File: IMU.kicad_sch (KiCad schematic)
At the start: 12 parts, among them U5 H3LIS331DLTR, U6 MMC5983MA, U7 ICM-20608-G

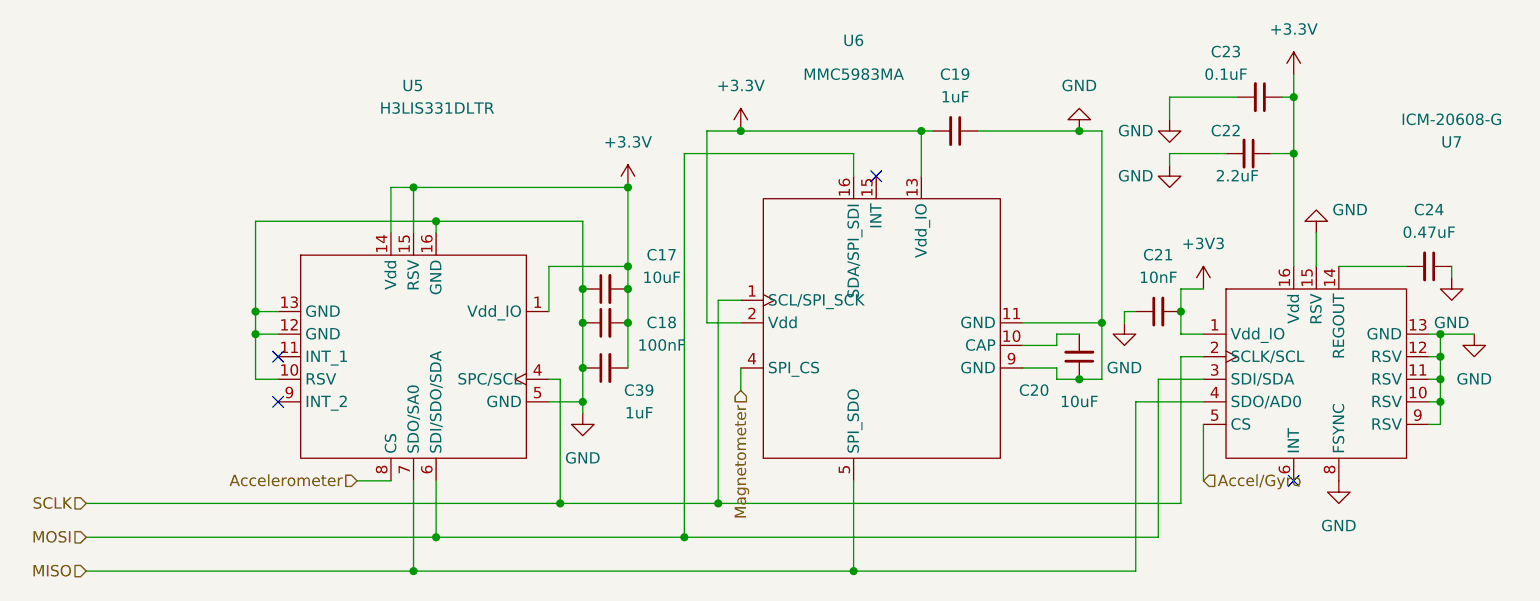
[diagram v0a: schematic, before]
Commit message: rerouted spi bus and changed NAND
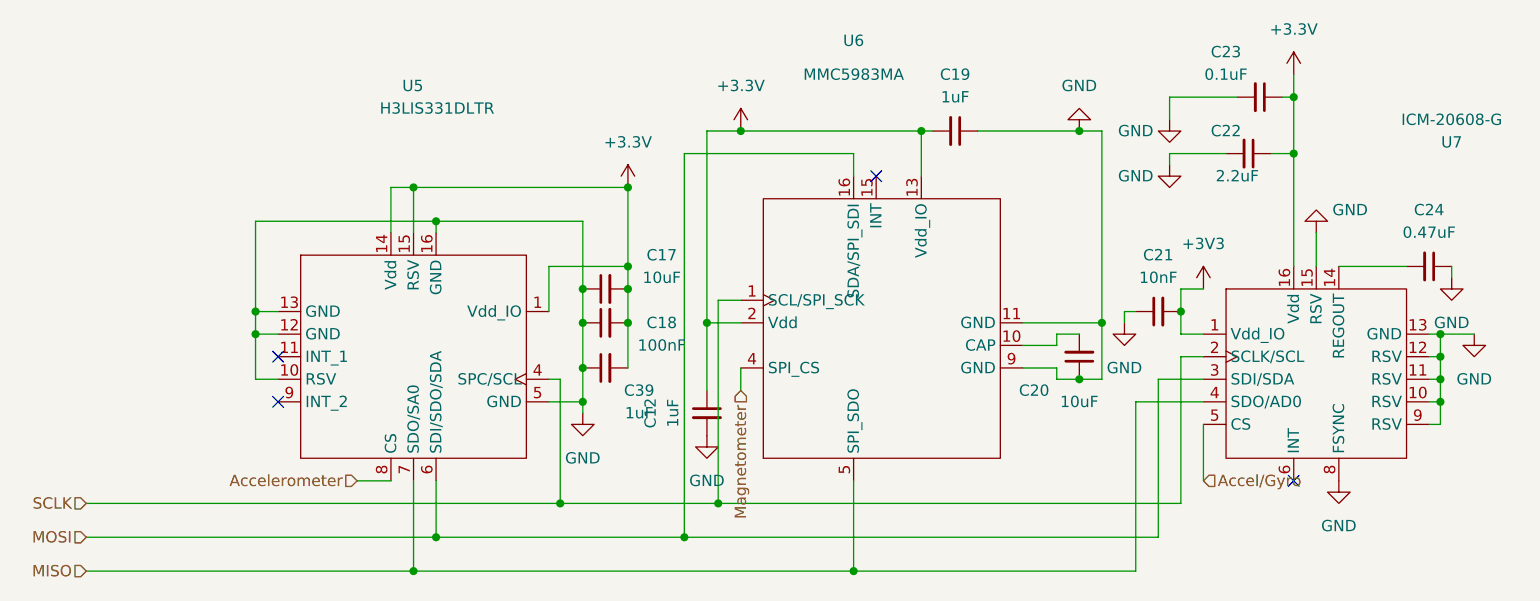
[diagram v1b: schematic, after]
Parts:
- added C12: 1uF, Capacitor_SMD:C_0402_1005Metric, symbol Device:C_Small
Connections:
- net +3V3: now also C12.1
- net GND: now also C12.2
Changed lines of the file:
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@@
   (junction (at 90.17 118.11) (diameter 0) (color 0 0 0 0)
+  )
+  (junction (at 120.65 93.98) (diameter 0) (color 0 0 0 0)
   )
   (junction (at 186.69 74.93) (diameter 0) (color 0 0 0 0)
@@
     (stroke (width 0) (type default))
   )
-  (wire (pts (xy 120.65 93.98) (xy 120.65 72.39))
-    (stroke (width 0) (type default))
-  )
   (wire (pts (xy 102.87 102.87) (xy 106.68 102.87))
     (stroke (width 0) (type default))
@@
     (stroke (width 0) (type default))
   )
+  (wire (pts (xy 120.65 72.39) (xy 120.65 93.98))
+    (stroke (width 0) (type default))
+  )
   (wire (pts (xy 90.17 83.82) (xy 90.17 82.55))
     (stroke (width 0) (type default))
@@
   )
   (wire (pts (xy 167.64 92.71) (xy 167.64 93.98))
+    (stroke (width 0) (type default))
+  )
+  (wire (pts (xy 120.65 93.98) (xy 120.65 101.6))
     (stroke (width 0) (type default))
   )
@@
     (pin "2")
     (instances
-      (project "Altimeter"
+      (project "Altimeter_super_thin"
         (path "/7db990e4-92e1-4f99-b4d2-435bbec1ba83/4373f5d0-1e9d-489b-aa26-9288beeb8cb3"
           (reference "C22") (unit 1)
@@
     (pin "2")
     (instances
-      (project "Altimeter"
+      (project "Altimeter_super_thin"
         (path "/7db990e4-92e1-4f99-b4d2-435bbec1ba83/4373f5d0-1e9d-489b-aa26-9288beeb8cb3"
           (reference "C21") (unit 1)
@@
     (pin "9")
     (instances
-      (project "Altimeter"
+      (project "Altimeter_super_thin"
         (path "/7db990e4-92e1-4f99-b4d2-435bbec1ba83/4373f5d0-1e9d-489b-aa26-9288beeb8cb3"
           (reference "U7") (unit 1)
@@
     (pin "1")
     (instances
-      (project "Altimeter"
+      (project "Altimeter_super_thin"
         (path "/7db990e4-92e1-4f99-b4d2-435bbec1ba83/4373f5d0-1e9d-489b-aa26-9288beeb8cb3"
           (reference "#PWR048") (unit 1)
@@
     (pin "2")
     (instances
-      (project "Altimeter"
+      (project "Altimeter_super_thin"
         (path "/7db990e4-92e1-4f99-b4d2-435bbec1ba83/4373f5d0-1e9d-489b-aa26-9288beeb8cb3"
           (reference "C24") (unit 1)
@@
     (pin "1")
     (instances
-      (project "Altimeter"
+      (project "Altimeter_super_thin"
         (path "/7db990e4-92e1-4f99-b4d2-435bbec1ba83/4373f5d0-1e9d-489b-aa26-9288beeb8cb3"
           (reference "#PWR050") (unit 1)
@@
     (pin "1")
     (instances
-      (project "Altimeter"
+      (project "Altimeter_super_thin"
         (path "/7db990e4-92e1-4f99-b4d2-435bbec1ba83/4373f5d0-1e9d-489b-aa26-9288beeb8cb3"
           (reference "#PWR049") (unit 1)
@@
     (pin "1")
     (instances
-      (project "Altimeter"
+      (project "Altimeter_super_thin"
         (path "/7db990e4-92e1-4f99-b4d2-435bbec1ba83/4373f5d0-1e9d-489b-aa26-9288beeb8cb3"
           (reference "#PWR040") (unit 1)
@@
     (pin "9")
     (instances
-      (project "Altimeter"
+      (project "Altimeter_super_thin"
         (path "/7db990e4-92e1-4f99-b4d2-435bbec1ba83/4373f5d0-1e9d-489b-aa26-9288beeb8cb3"
           (reference "U6") (unit 1)
@@
     (pin "2")
     (instances
-      (project "Altimeter"
+      (project "Altimeter_super_thin"
         (path "/7db990e4-92e1-4f99-b4d2-435bbec1ba83/4373f5d0-1e9d-489b-aa26-9288beeb8cb3"
           (reference "C23") (unit 1)
@@
     )
   )
+  (symbol (lib_id "power:GND") (at 120.65 106.68 0) (unit 1)
+    (in_bom yes) (on_board yes) (dnp no) (fields_autoplaced)
+    (property "Reference" "#PWR08" (at 120.65 113.03 0)
+      (effects (font (size 1.27 1.27)) hide)
+    )
+    (property "Value" "GND" (at 120.65 111.76 0)
+      (effects (font (size 1.27 1.27)))
+    )
+    (property "Footprint" "" (at 120.65 106.68 0)
+      (effects (font (size 1.27 1.27)) hide)
+    )
+    (property "Datasheet" "" (at 120.65 106.68 0)
+      (effects (font (size 1.27 1.27)) hide)
+    )
+    (pin "1")
+    (instances
+      (project "Altimeter_super_thin"
+        (path "/7db990e4-92e1-4f99-b4d2-435bbec1ba83/4373f5d0-1e9d-489b-aa26-9288beeb8cb3"
+          (reference "#PWR08") (unit 1)
+        )
+      )
+    )
+  )
   (symbol (lib_id "Device:C_Small") (at 109.22 99.06 90) (unit 1)
     (in_bom yes) (on_board yes) (dnp no)
@@
     (pin "2")
     (instances
-      (project "Altimeter"
+      (project "Altimeter_super_thin"
         (path "/7db990e4-92e1-4f99-b4d2-435bbec1ba83/4373f5d0-1e9d-489b-aa26-9288beeb8cb3"
           (reference "C39") (unit 1)
@@
     (pin "1")
     (instances
-      (project "Altimeter"
+      (project "Altimeter_super_thin"
         (path "/7db990e4-92e1-4f99-b4d2-435bbec1ba83/4373f5d0-1e9d-489b-aa26-9288beeb8cb3"
           (reference "#PWR041") (unit 1)
@@
     (pin "2")
     (instances
-      (project "Altimeter"
+      (project "Altimeter_super_thin"
         (path "/7db990e4-92e1-4f99-b4d2-435bbec1ba83/4373f5d0-1e9d-489b-aa26-9288beeb8cb3"
           (reference "C19") (unit 1)
@@
     (pin "1")
     (instances
-      (project "Altimeter"
+      (project "Altimeter_super_thin"
         (path "/7db990e4-92e1-4f99-b4d2-435bbec1ba83/4373f5d0-1e9d-489b-aa26-9288beeb8cb3"
           (reference "#PWR042") (unit 1)
@@
     (pin "2")
     (instances
-      (project "Altimeter"
+      (project "Altimeter_super_thin"
         (path "/7db990e4-92e1-4f99-b4d2-435bbec1ba83/4373f5d0-1e9d-489b-aa26-9288beeb8cb3"
           (reference "C20") (unit 1)
@@
     (pin "2")
     (instances
-      (project "Altimeter"
+      (project "Altimeter_super_thin"
         (path "/7db990e4-92e1-4f99-b4d2-435bbec1ba83/4373f5d0-1e9d-489b-aa26-9288beeb8cb3"
           (reference "C18") (unit 1)
@@
     (pin "1")
     (instances
-      (project "Altimeter"
+      (project "Altimeter_super_thin"
         (path "/7db990e4-92e1-4f99-b4d2-435bbec1ba83/4373f5d0-1e9d-489b-aa26-9288beeb8cb3"
           (reference "#PWR046") (unit 1)
@@
     (pin "1")
     (instances
-      (project "Altimeter"
+      (project "Altimeter_super_thin"
         (path "/7db990e4-92e1-4f99-b4d2-435bbec1ba83/4373f5d0-1e9d-489b-aa26-9288beeb8cb3"
           (reference "#PWR039") (unit 1)
@@
     (pin "1")
     (instances
-      (project "Altimeter"
+      (project "Altimeter_super_thin"
         (path "/7db990e4-92e1-4f99-b4d2-435bbec1ba83/4373f5d0-1e9d-489b-aa26-9288beeb8cb3"
           (reference "#PWR045") (unit 1)
@@
     (pin "1")
     (instances
-      (project "Altimeter"
+      (project "Altimeter_super_thin"
         (path "/7db990e4-92e1-4f99-b4d2-435bbec1ba83/4373f5d0-1e9d-489b-aa26-9288beeb8cb3"
           (reference "#PWR047") (unit 1)
@@
     (pin "1")
     (instances
-      (project "Altimeter"
+      (project "Altimeter_super_thin"
         (path "/7db990e4-92e1-4f99-b4d2-435bbec1ba83/4373f5d0-1e9d-489b-aa26-9288beeb8cb3"
           (reference "#PWR051") (unit 1)
@@
     )
   )
+  (symbol (lib_id "Device:C_Small") (at 120.65 104.14 0) (unit 1)
+    (in_bom yes) (on_board yes) (dnp no)
+    (property "Reference" "C12" (at 114.3 104.14 90)
+      (effects (font (size 1.27 1.27)))
+    )
+    (property "Value" "1uF" (at 116.84 104.14 90)
+      (effects (font (size 1.27 1.27)))
+    )
+    (property "Footprint" "Capacitor_SMD:C_0402_1005Metric" (at 120.65 104.14 0)
+      (effects (font (size 1.27 1.27)) hide)
+    )
+    (property "Datasheet" "~" (at 120.65 104.14 0)
+      (effects (font (size 1.27 1.27)) hide)
+    )
+    (pin "1")
+    (pin "2")
+    (instances
+      (project "Altimeter_super_thin"
+        (path "/7db990e4-92e1-4f99-b4d2-435bbec1ba83/4373f5d0-1e9d-489b-aa26-9288beeb8cb3"
+          (reference "C12") (unit 1)
+        )
+      )
+    )
+  )
   (symbol (lib_id "power:GND") (at 167.64 93.98 0) (unit 1)
     (in_bom yes) (on_board yes) (dnp no)
@@
     (pin "1")
     (instances
-      (project "Altimeter"
+      (project "Altimeter_super_thin"
         (path "/7db990e4-92e1-4f99-b4d2-435bbec1ba83/4373f5d0-1e9d-489b-aa26-9288beeb8cb3"
           (reference "#PWR043") (unit 1)
@@
     (pin "2")
     (instances
-      (project "Altimeter"
+      (project "Altimeter_super_thin"
         (path "/7db990e4-92e1-4f99-b4d2-435bbec1ba83/4373f5d0-1e9d-489b-aa26-9288beeb8cb3"
           (reference "C17") (unit 1)
@@
     (pin "9")
     (instances
-      (project "Altimeter"
+      (project "Altimeter_super_thin"
         (path "/7db990e4-92e1-4f99-b4d2-435bbec1ba83/4373f5d0-1e9d-489b-aa26-9288beeb8cb3"
           (reference "U5") (unit 1)
@@
     (pin "1")
     (instances
-      (project "Altimeter"
+      (project "Altimeter_super_thin"
         (path "/7db990e4-92e1-4f99-b4d2-435bbec1ba83/4373f5d0-1e9d-489b-aa26-9288beeb8cb3"
           (reference "#PWR044") (unit 1)
